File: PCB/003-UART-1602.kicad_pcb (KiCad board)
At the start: 2 copper layers, 18 parts, among them J1 CONN_POWER, J2 CONN_DATA, Q1 AO3400A, Q2 AO3400A, SW1 BAUD_SEL, U1 CH32V003

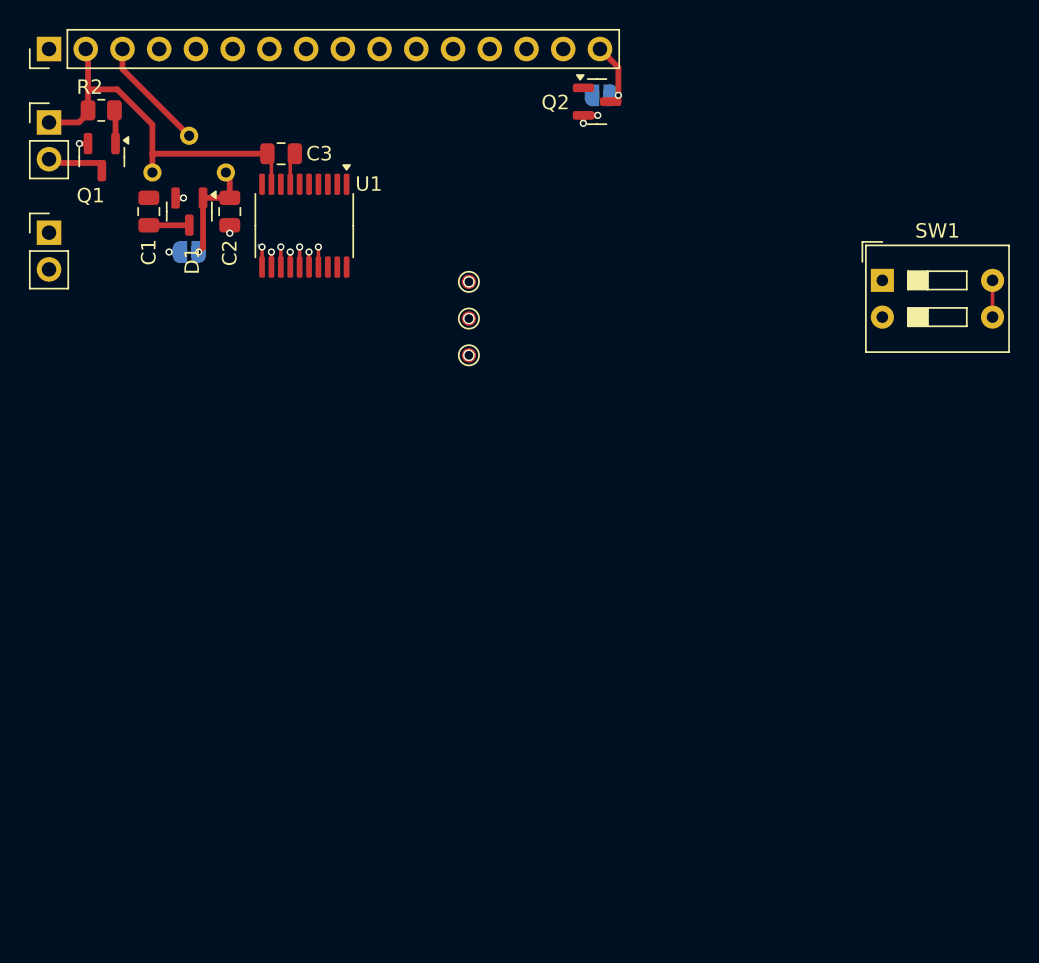
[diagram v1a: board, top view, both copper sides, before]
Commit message: Added DIP Switch to PCB
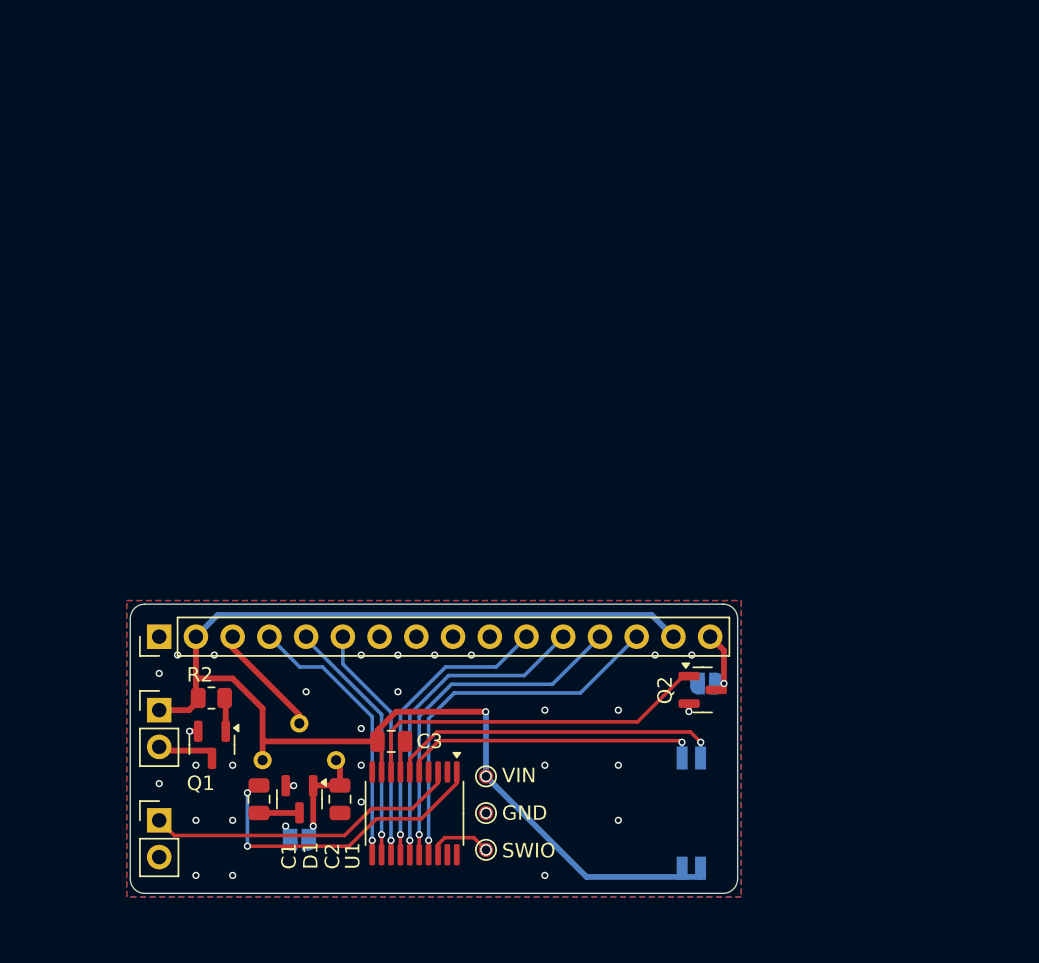
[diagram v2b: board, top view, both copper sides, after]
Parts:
- SW1: footprint Button_Switch_THT:SW_DIP_SPSTx02_Slide_9.78x7.26mm_W7.62mm_P2.54mm -> Button_Switch_SMD:SW_DIP_SPSTx02_Slide_Copal_CHS-02B_W7.62mm_P1.27mm; moved to B.Cu
- moved JP1 41.3 mm to (42.7, 77.5)
- moved Q1 41.3 mm to (36.7, 71.0)
- moved RV1 41.3 mm to (45.2, 72.0)
- moved DS1 41.3 mm to (33.0, 63.5)
- moved J1 41.3 mm to (33.0, 68.6)
- moved J2 41.3 mm to (33.0, 76.2)
- moved U1 41.3 mm to (50.7, 75.7)
- moved C1 41.3 mm to (39.9, 74.7)
- moved C2 41.3 mm to (45.5, 74.7)
- moved C3 41.3 mm to (49.1, 70.7)
- moved D1 41.3 mm to (42.7, 74.7)
- moved R2 41.3 mm to (36.6, 67.7)
- moved JP2 41.3 mm to (70.9, 66.7)
- moved Q2 41.3 mm to (70.6, 67.2)
- moved SW1 39.1 mm to (69.8, 75.7), turned to -90 degrees
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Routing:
- net /VBUS_VIN: track 29.0 -> 92.5 mm, vias 1 -> 2
- net /LCD_BL: track 0.00 -> 25.0 mm
- net /LCD_DA_3: track 1.39 -> 26.1 mm
- net /LCD_DA_2: track 1.04 -> 24.3 mm
- net /BAUD_SEL1: track 0.00 -> 23.2 mm, vias 0 -> 1
- net /UART_RX: track 0.00 -> 22.0 mm
- net /CHRGPMP: track 0.00 -> 21.8 mm, vias 0 -> 2
- net /LCD_DA_1: track 1.39 -> 22.5 mm
- net /BAUD_SEL0: track 0.00 -> 20.7 mm, vias 0 -> 1
- net /LCD_DA_0: track 1.04 -> 20.7 mm
- net /LCD_RS: track 2.39 -> 18.9 mm
- net /LCD_RW: track 1.04 -> 17.2 mm
- net /LCD_EN: track 1.39 -> 16.5 mm
- net /SWIO: track 0.00 -> 4.57 mm
- net GND: track 6.24 -> 5.02 mm, vias 7 -> 32
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- added copper zone on B.Cu, net GND
- added copper zone on F.Cu, net GND
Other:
- board outline added: 42 x 20 mm
- board text added: "0"
- board text added: "1"
- board text added: "115200"
- board text added: "460800"
- board text added: "4800"
- board text added: "9600"
- board text added: "A"
- board text added: "B"
- board text added: "BAUD"

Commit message: Almost Final PCB
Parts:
- JP1: value JMP_V0_GND -> JMP_V0
- JP2: value JMP_BL_GND -> JMP_BL
- moved JP2 0.70 mm to (70.2, 66.7)
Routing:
- net /VBUS_VIN: track 92.5 -> 91.6 mm
- net Net-(DS1-LED(-)): track 6.10 -> 6.73 mm
- net /LCD_DA_3: track 26.1 -> 25.5 mm
- net /LCD_DA_2: track 24.3 -> 23.7 mm
- net /UART_RX: track 22.0 -> 21.4 mm
- net /LCD_DA_1: track 22.5 -> 22.0 mm
- net /LCD_DA_0: track 20.7 -> 20.2 mm
- net /CHRGPMP: track 21.8 -> 21.2 mm
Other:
- board text added: "003-UART-1602 17 Dec 2024 MkI"

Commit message: PCB Finished
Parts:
- moved C1 2.62 mm to (39.3, 77.3)
- moved C2 2.62 mm to (44.9, 77.3)
- moved C3 2.62 mm to (48.4, 73.3)
- moved R2 2.62 mm to (36.0, 70.3)
- moved D1 2.62 mm to (42.1, 77.3)
- moved JP2 2.62 mm to (69.6, 69.3)
- moved Q2 2.62 mm to (70.0, 69.7)
- moved DS1 2.62 mm to (32.4, 66.0)
- moved J1 2.62 mm to (32.4, 71.1)
- moved J2 2.62 mm to (32.4, 78.7)
- moved Q1 2.62 mm to (36.0, 73.5)
- moved RV1 2.62 mm to (44.6, 74.6)
- moved U1 2.62 mm to (50.0, 78.3)
- moved JP1 2.62 mm to (42.1, 80.1)
- moved SW1 2.62 mm to (69.2, 78.2)
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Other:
- board text added: "B+"
- board text added: "B-"
- board text added: "GND"
- board text added: "RX"
